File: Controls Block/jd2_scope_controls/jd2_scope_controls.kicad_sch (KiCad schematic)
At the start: 5 parts, among them SW1 RotaryEncoder_Switch

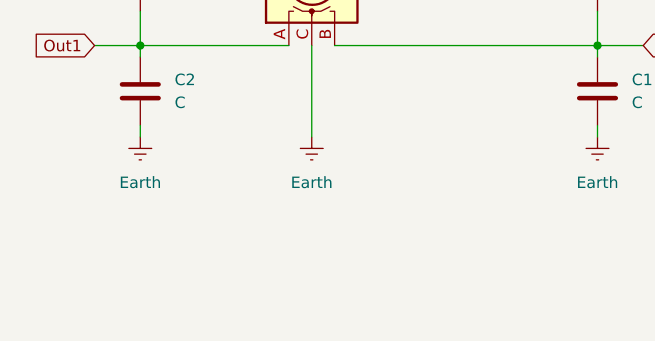
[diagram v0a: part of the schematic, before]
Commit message: first footprint added
+ some other stuff for controls
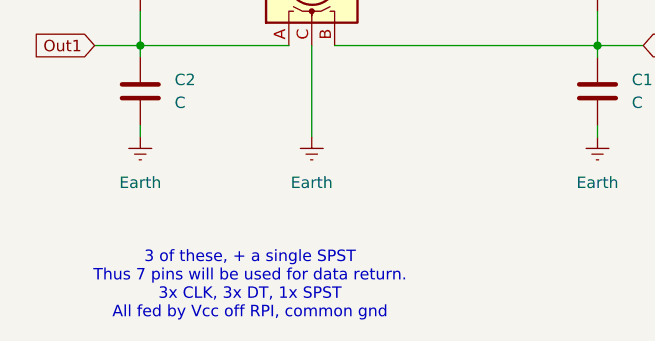
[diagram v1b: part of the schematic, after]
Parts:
- SW1: footprint (none) -> Rotary_Encoder:RotaryEncoder_Alps_EC11E-Switch_Vertical_H20mm
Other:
- note added: "3 of these, + a single SPST Thus 7 pins will be used for data return. 3x CLK, 3x DT, 1x SPST All fed by Vcc off RPI, common gnd"
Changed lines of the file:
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@@
 	(generator_version "9.0")
 	(paper "A4")
+	(text "3 of these, + a single SPST\nThus 7 pins will be used for data return.\n3x CLK, 3x DT, 1x SPST\nAll fed by Vcc off RPI, common gnd"
+		(exclude_from_sim no)
+		(at 202.692 116.84 0)
+		(effects
+			(font
+				(size 1.27 1.27)
+			)
+		)
+	)
 	(junction
 		(at 190.5 90.17)
@@
 			)
 		)
-		(property "Footprint" ""
+		(property "Footprint" "Rotary_Encoder:RotaryEncoder_Alps_EC11E-Switch_Vertical_H20mm"
 			(at 205.486 86.36 0)
 			(effects

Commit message: component values
:P
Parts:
- C1, C2: value C -> 1u
- R1, R2: value R_US -> 10k
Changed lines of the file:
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@@
 			)
 		)
-		(property "Value" "R_US"
+		(property "Value" "10k"
 			(at 243.84 83.8199 0)
 			(effects
@@
 			)
 		)
-		(property "Value" "R_US"
+		(property "Value" "10k"
 			(at 193.04 83.8199 0)
 			(effects
@@
 			)
 		)
-		(property "Value" "C"
+		(property "Value" "1u"
 			(at 245.11 96.5199 0)
 			(effects
@@
 			)
 		)
-		(property "Value" "C"
+		(property "Value" "1u"
 			(at 194.31 96.5199 0)
 			(effects

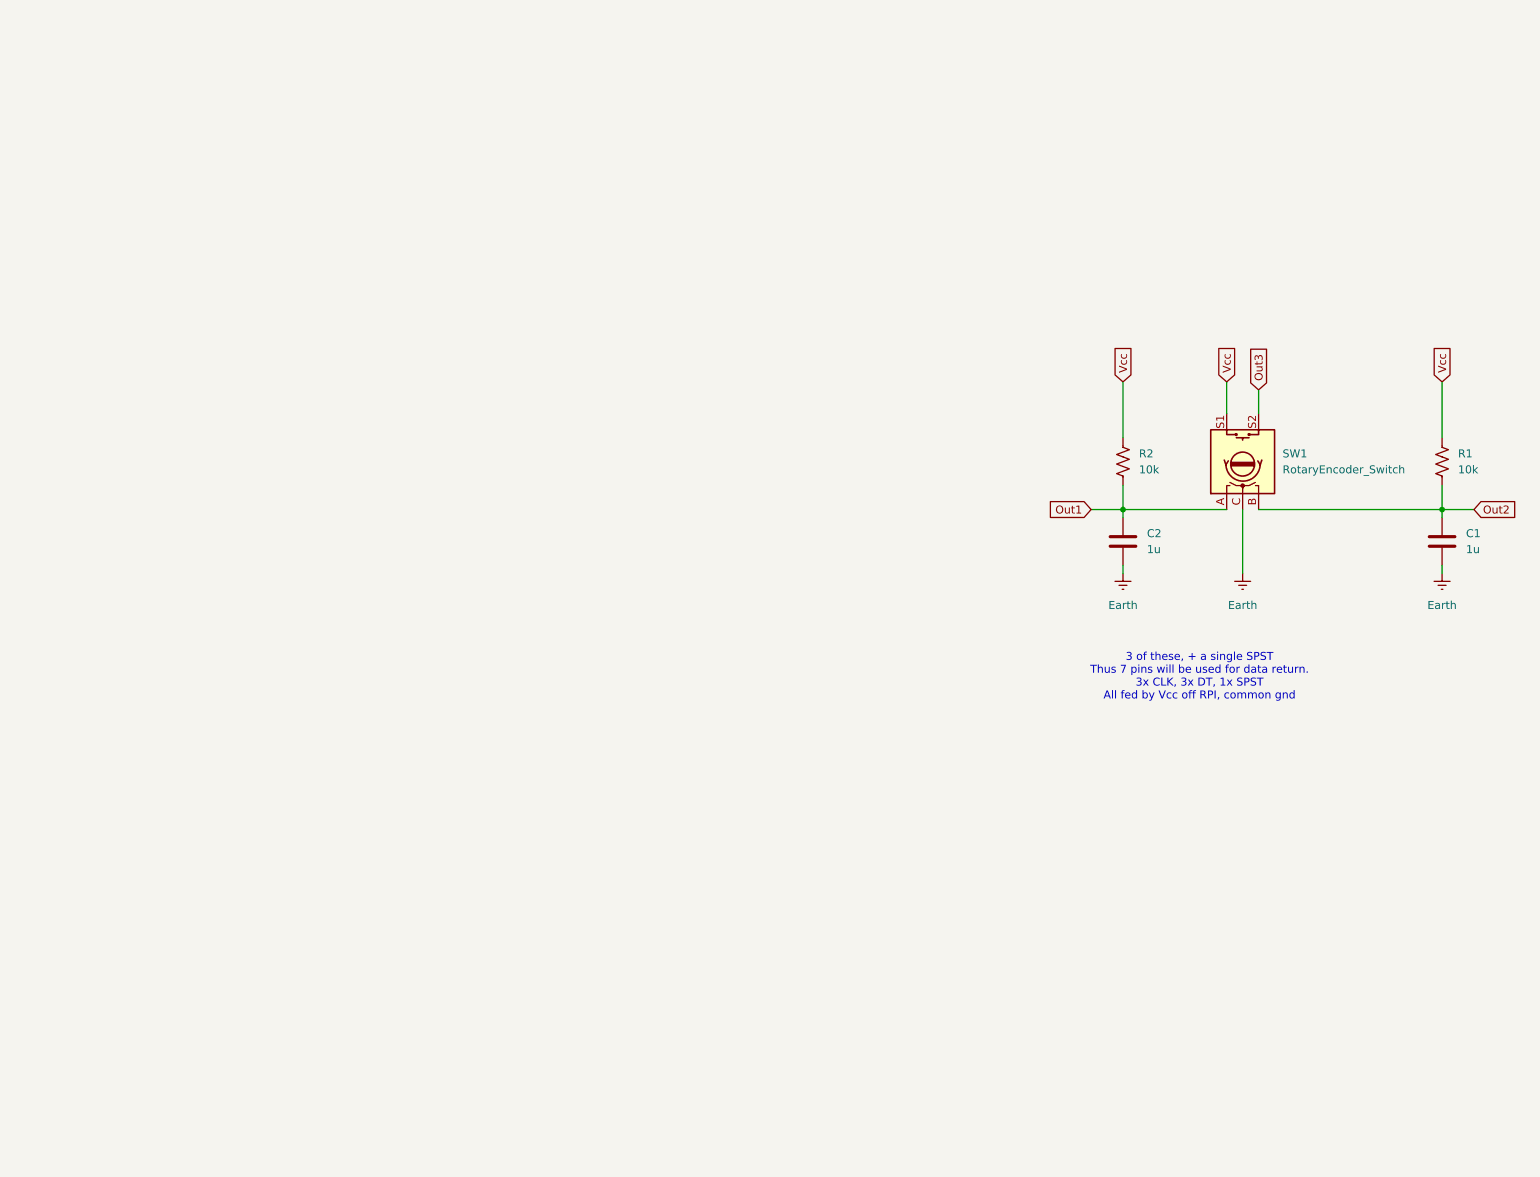
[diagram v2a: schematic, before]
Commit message: updated controls schem
full design incorporated.
still needs full PCB layout and footprints
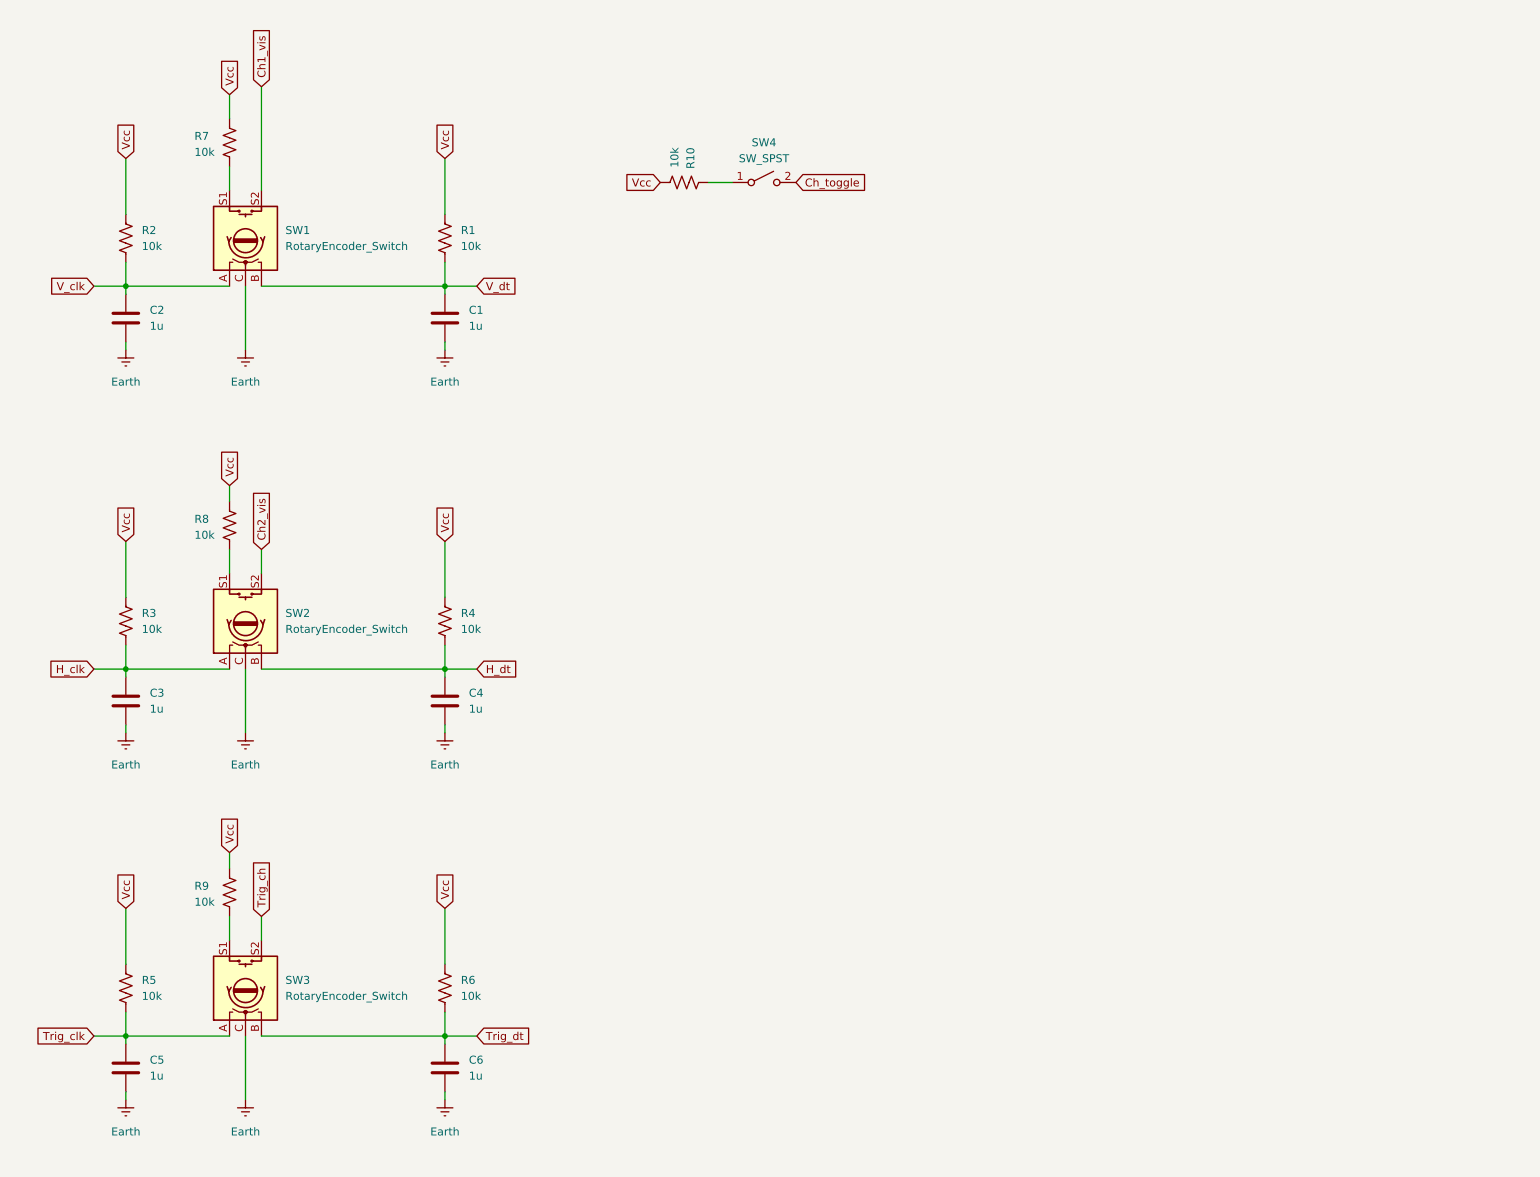
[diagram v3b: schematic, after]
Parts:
- added C3, C4, C5, C6: 1u, symbol Device:C
- added R10, R3, R4, R5, R6, R7, R8, R9: 10k, symbol Device:R_US
- added SW2, SW3: RotaryEncoder_Switch, Rotary_Encoder:RotaryEncoder_Alps_EC11E-Switch_Vertical_H20mm, symbol Device:RotaryEncoder_Switch
- added SW4: SW_SPST, symbol Switch:SW_SPST
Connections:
- net Earth: now also C3.2, C4.2, C5.2, C6.2, SW2.C, SW3.C
- net Vcc: now also R10.2, R3.1, R4.1, R5.1, R6.1, R7.1, R8.1, R9.1; no longer SW1.S1
- net Out1 renamed V_clk
- net Out2 renamed V_dt
- net Out3 renamed Ch1_vis
- new net: R9.2, SW3.S1
- new net: R8.2, SW2.S1
- new net: R10.1, SW4.1 (A)
- new net: R7.2, SW1.S1
- new net Ch2_vis: SW2.S2
- new net Ch_toggle: SW4.2 (B)
- new net H_clk: C3.1, R3.2, SW2.A
- new net H_dt: C4.1, R4.2, SW2.B
- new net Trig_ch: SW3.S2
- new net Trig_clk: C5.1, R5.2, SW3.A
- new net Trig_dt: C6.1, R6.2, SW3.B
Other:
- note removed: "3 of these, + a single SPST Thus 7 pins will be used for data return. 3x CLK, 3x DT, 1x SPST All fed by Vcc off RPI, common gnd"
- moved on the sheet: C1, C2, R1, R2, SW1

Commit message: footprint stuff
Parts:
- removed C1, C2, C3, C4, C5, C6: 1u, symbol Device:C
- removed R1, R10, R2, R3, R4, R5, R6, R7, R8, R9: 10k, symbol Device:R_US
- added C1, C2, C3, C4, C7, C8: 1u, CAP_UEP_6P3X11_NCH, symbol fp1:UVZ2F010MED1TD
- added R1, R11, R2, R3, R4, R5, R6, R7, R8: 10k, STA_RMCF0402_STP, symbol fp1:RMCF0402FT10K0
- SW4: footprint (none) -> Button_Switch_SMD:Nidec_Copal_CAS-120A
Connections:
- net Ch2_vis is gone; now on net Ch1_vis: SW2.S2
- net H_clk is gone; now on net V_clk: SW2.A
- net H_dt is gone; now on net V_dt: SW2.B
- net Trig_ch is gone; now on net Ch1_vis: SW3.S2
- net Trig_clk is gone; now on net V_clk: SW3.A
- net Trig_dt is gone; now on net V_dt: SW3.B
- net Earth: now also C1.1, C2.1, C3.1, C4.1, C7.1, C8.1
- net V_clk: now also C1.2, C3.2, C7.2, R11.1, R3.1, R6.1
- net V_dt: now also C2.2, C4.2, C8.2, R2.1, R5.1, R8.1
- net Vcc: now also R1.2, R11.2, R2.2, R3.2, R4.2, R5.2, R6.2, R7.2, R8.2
- net at SW3.S1: now also R7.1
- net at SW2.S1: now also R4.1
- net at SW1.S1: now also R1.1
